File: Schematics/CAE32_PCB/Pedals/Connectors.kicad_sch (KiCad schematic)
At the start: 6 parts, among them J15 USB_C_Receptacle_USB2.0

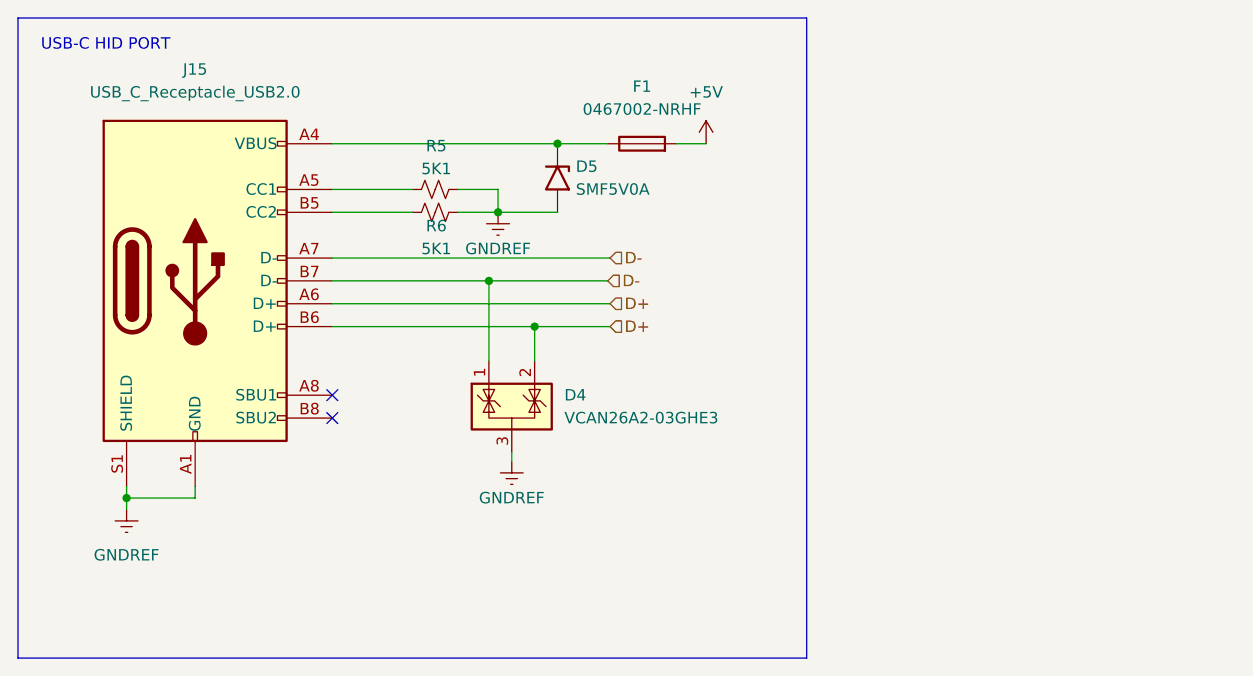
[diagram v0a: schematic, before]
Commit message: updated: Pcb design, fixed plane grounds and minor improvements, added stlink connector, updated BOM with the current market stock
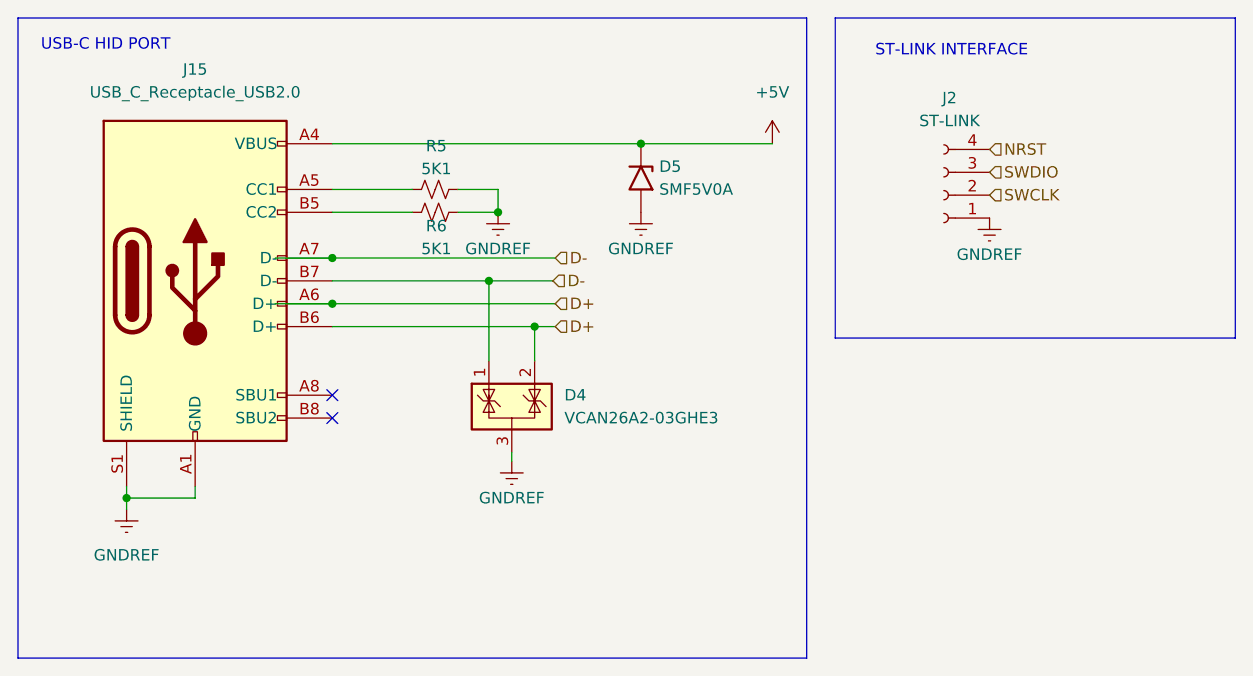
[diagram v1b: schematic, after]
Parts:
- removed F1: 0467002-NRHF, Fuse:Fuse_0603_1608Metric, symbol Device:Fuse
- added J2: ST-LINK, Connector_PinSocket_2.54mm:PinSocket_1x04_P2.54mm_Vertical, symbol Connector:Conn_01x04_Socket
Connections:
- net +5V: now also D5.1 (A1), J15.A4 (VBUS), J15.A9 (VBUS), J15.B4 (VBUS), J15.B9 (VBUS)
- net GNDREF: now also J2.1 (Pin_1)
- new net NRST: J2.4 (Pin_4)
- new net SWCLK: J2.2 (Pin_2)
- new net SWDIO: J2.3 (Pin_3)
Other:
- note added: "ST-LINK INTERFACE"
- moved on the sheet: D5
